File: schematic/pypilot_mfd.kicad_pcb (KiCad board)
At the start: 2 copper layers, 115.8 x 85.9 mm, 94 parts, among them J1 usb, J2 keypad, J3 Conn_01x02, J4 Conn_01x02, J5 jlx256160, J6 usb, Q1 Q_PMOS_GSD, Q2 Q_PMOS_GSD, Q3 Q_PMOS_DSG, Q4 Q_NMOS_GSD, U1 CH340G, U10 24LC512, U11 LMR50410, U12 AP2127K-ADJ, U2 AMS1117-3.3, U3 ESP32-WROOM-32D, U4 SN65220, U5 ADM2587E, U6 LIS2DE12, U7 74AHC04, U8 BUZZER-freetronics_schematic, U9 LIS2DE12, Y1 12mhz

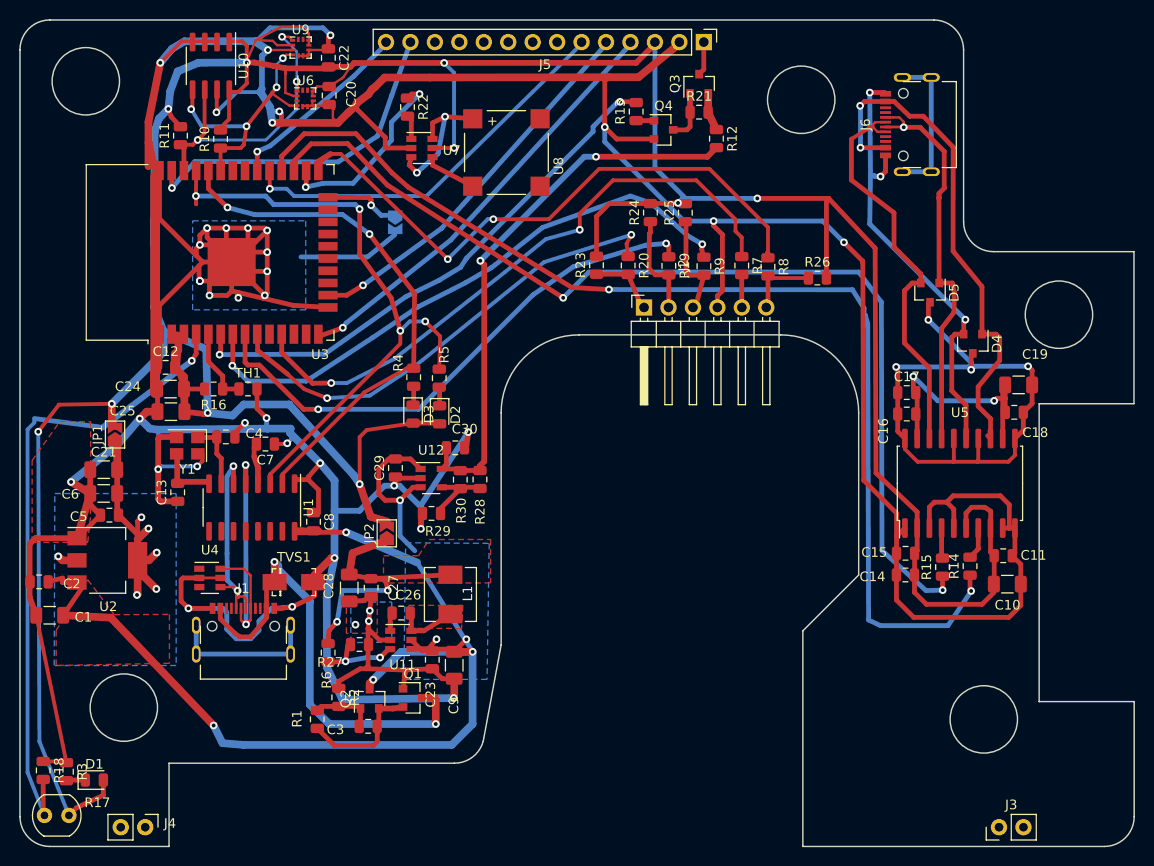
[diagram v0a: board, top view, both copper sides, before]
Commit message: add schematics and models for sensors
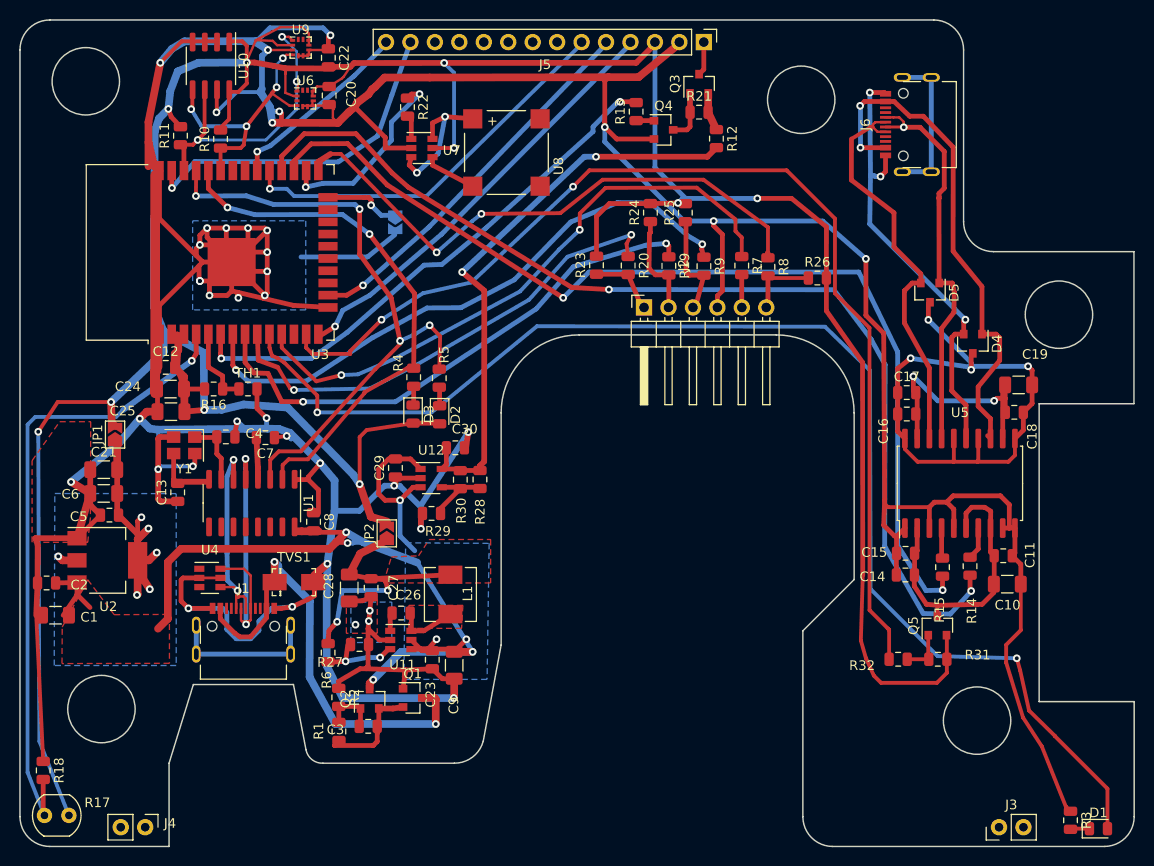
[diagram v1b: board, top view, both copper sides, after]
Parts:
- added Q5: Q_PMOS_DSG, pypilot_footprints:SOT-23_180, F.Cu at (108.1, 77.0)
- added R31: 100k, Resistor_SMD:R_0805_2012Metric, F.Cu at (108.2, 80.5)
- added R32: 10k, Resistor_SMD:R_0805_2012Metric, F.Cu at (104.0, 80.5)
- moved D1 104.4 mm to (124.9, 98.2)
- moved R3 104.4 mm to (122.0, 97.3)
- moved R1 2.58 mm to (46.0, 88.0)
- moved C2 0.78 mm to (15.6, 72.6)
- moved C7 0.67 mm to (38.3, 57.5)
- moved C1 0.60 mm to (16.5, 76.0)
- moved U1 0.46 mm to (36.9, 64.1)
- moved Y1 0.32 mm to (29.9, 58.3)
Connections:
- C10 pad 2: +3V3 -> Net-(C10-Pad2)
- C11 pad 2: +3V3 -> Net-(C10-Pad2)
- C14 pad 2: +3V3 -> Net-(C10-Pad2)
- C15 pad 2: +3V3 -> Net-(C10-Pad2)
- D1 pad 2: +3V3 -> LEDS_VCC
- U3 pad 10: Net-(U3-Pad10) -> LEDS_VCC
- U3 pad 13: Net-(U3-Pad13) -> RS422_PWR
- U5 pad 2: +3V3 -> Net-(C10-Pad2)
- U5 pad 6: +3V3 -> Net-(C10-Pad2)
- U5 pad 8: +3V3 -> Net-(C10-Pad2)
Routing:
- net LEDS_VCC: track 0.00 -> 134.8 mm, vias 0 -> 2
- net RS422_PWR: track 0.00 -> 114.2 mm, vias 0 -> 2
- net Net-(C10-Pad2): track 0.00 -> 30.2 mm
- net +5V: track 134.3 -> 109.4 mm
- net +3V3: track 396.0 -> 374.6 mm
- net TX1: track 116.3 -> 109.2 mm
- net GND: track 660.8 -> 667.8 mm
- net Net-(Q5-Pad1): track 0.00 -> 4.78 mm
- net PWR: track 62.5 -> 60.2 mm
- net Net-(C30-Pad2): track 58.0 -> 59.9 mm
- net Net-(C3-Pad2): track 14.2 -> 12.4 mm
- net RX: track 54.5 -> 55.9 mm
- net PWR_LED: track 64.4 -> 63.0 mm
- net Net-(J1-PadA6): track 29.2 -> 30.5 mm
- net Net-(J1-PadA7): track 21.2 -> 22.4 mm
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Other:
- outline, holes or cut-outs redrawn

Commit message: update enclosures and schematics
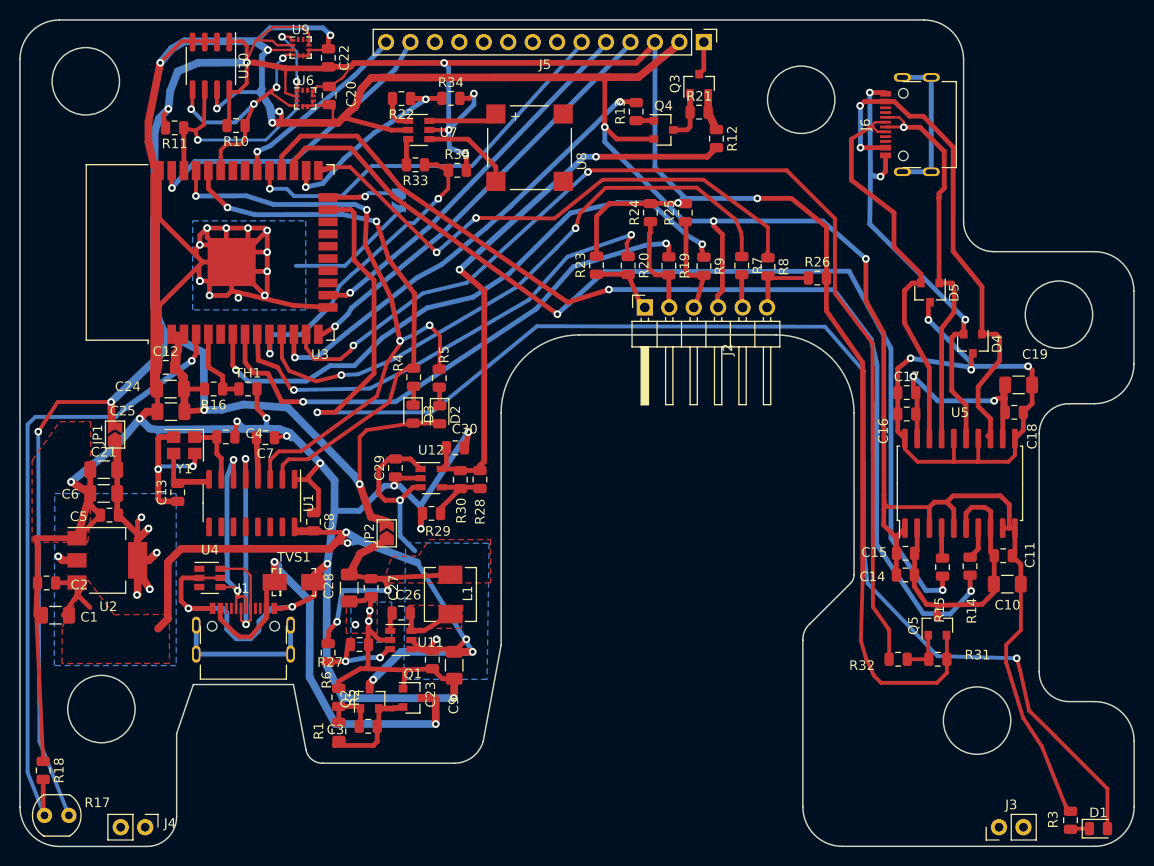
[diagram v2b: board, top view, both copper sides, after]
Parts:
- added R33: 1.2k, Resistor_SMD:R_0805_2012Metric, F.Cu at (53.9, 29.2)
- added R34: 100k, Resistor_SMD:R_0805_2012Metric, F.Cu at (57.6, 22.3)
- added R35: 100k, Resistor_SMD:R_0805_2012Metric, F.Cu at (58.2, 29.8)
- JP3: value Jumper -> Screen Mirrored
- Q3, Q5: value Q_PMOS_DSG -> Q_PMOS_GSD
- U11: footprint Package_TO_SOT_SMD:SOT-23-6 -> pypilot_footprints:SOT-23-6_180
- moved U8 2.45 mm to (65.8, 27.4)
- moved JP3 2.33 mm to (52.2, 32.9)
- moved R10 2.13 mm to (35.3, 25.1), turned to 180 degrees
- moved U7 1.90 mm to (54.2, 25.6)
- moved R22 1.08 mm to (52.5, 22.3), turned to 180 degrees
- moved R11 1.02 mm to (28.9, 25.3), turned to 180 degrees
- moved J2 0.08 mm to (84.1, 44.0), turned to 180 degrees
- turned U11 to 180 degrees
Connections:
- net BUZZER renamed BUZZERA
- U3 pad 10: LEDS_VCC -> BUZZERB
- U3 pad 12: CS_SD -> LEDA
- U3 pad 23: Net-(U3-Pad23) -> LEDS_VCC
- U3 pad 6: LEDA -> Net-(U3-Pad6)
- U7 pad 3: Net-(U7-Pad3) -> Net-(R33-Pad2)
- U7 pad 6: Net-(U7-Pad3) -> Net-(U7-Pad6)
- U8 pad 1: Net-(U7-Pad3) -> Net-(U7-Pad6)
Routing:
- net BUZZERB: track 0.00 -> 33.4 mm, vias 0 -> 2
- net LEDS_VCC: track 134.8 -> 152.1 mm
- net Net-(U7-Pad3): track 14.8 -> 0.00 mm, vias 2 -> 0
- net +3V3: track 374.6 -> 383.8 mm, vias 10 -> 12
- net LEDA: track 56.0 -> 47.8 mm
- net Net-(U7-Pad6): track 0.00 -> 7.20 mm
- net Net-(U7-Pad4): track 5.54 -> 9.60 mm
- net Net-(R33-Pad2): track 0.00 -> 2.74 mm
- net MOSI: track 35.7 -> 33.2 mm
- net BUZZERA: track 20.1 -> 22.3 mm
- net GND: track 667.8 -> 665.8 mm
- net PWR: track 60.2 -> 58.5 mm
- net RX: track 55.9 -> 57.2 mm
- net TX1: track 109.2 -> 110.4 mm
- net SDA: track 28.9 -> 30.0 mm
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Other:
- outline, holes or cut-outs redrawn

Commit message: add foot prints
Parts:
- removed D1: LED3, LED_SMD:LED_0805_2012Metric
- removed JP2: Jumper, Jumper:SolderJumper-2_P1.3mm_Open_TrianglePad1.0x1.5mm
- added C31: 10uF, Capacitor_SMD:C_1206_3216Metric, F.Cu at (51.1, 68.0)
- added Q6: Q_NMOS_GSD, pypilot_footprints:SOT-23_180, F.Cu at (103.5, 85.9)
- added R36: 1.2k, Resistor_SMD:R_0805_2012Metric, F.Cu at (89.6, 73.8)
- added R37: 4.7, Resistor_SMD:R_0805_2012Metric, F.Cu at (99.3, 87.0)
- R3: value 1.5k -> 1.2k
- moved R3 36.0 mm to (95.2, 73.1), turned to 0 degrees
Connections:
- Q5 pad 2: +3V3 -> Net-(Q5-Pad2)
- R14 pad 1: TX1 -> TX2
- R15 pad 1: RX1 -> GND
- R3 pad 1: GND -> Net-(R3-Pad1)
- R3 pad 2: Net-(D1-Pad1) -> Net-(R3-Pad2)
- R31 pad 2: +3V3 -> Net-(Q5-Pad2)
- R32 pad 2: Net-(Q5-Pad1) -> Net-(Q6-Pad1)
- U3 pad 23: LEDS_VCC -> RX1
- U3 pad 24: Net-(JP3-Pad1) -> TX1
- U3 pad 27: RX1 -> RX2
- U3 pad 28: TX1 -> TX2
- U3 pad 6: Net-(U3-Pad6) -> Net-(JP3-Pad1)
- U5 pad 4: Net-(R15-Pad2) -> Net-(R3-Pad2)
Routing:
- net LEDS_VCC: track 152.1 -> 0.00 mm, vias 2 -> 0
- net TX2: track 0.00 -> 110.4 mm, vias 0 -> 2
- net TX1: track 110.4 -> 0.00 mm, vias 2 -> 0
- net GND: track 665.8 -> 640.1 mm
- net +3V3: track 383.8 -> 366.7 mm
- net Net-(C27-Pad2): track 29.4 -> 23.8 mm
- net Net-(Q5-Pad2): track 0.00 -> 2.52 mm
- net Net-(Q5-Pad1): track 4.78 -> 2.53 mm
- net Net-(D1-Pad1): track 1.99 -> 0.00 mm

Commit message: update enclosure
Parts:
- removed JP3: Screen Mirrored, Jumper:SolderJumper-2_P1.3mm_Open_TrianglePad1.0x1.5mm
- added JP2: Jumper, Jumper:SolderJumper-2_P1.3mm_Open_TrianglePad1.0x1.5mm, B.Cu at (47.4, 57.8)
- added R38: 4.7, Resistor_SMD:R_0805_2012Metric, F.Cu at (98.1, 79.8)
- moved R36 23.0 mm to (112.5, 75.7), turned to 180 degrees
- moved R3 13.6 mm to (108.5, 70.5), turned to 90 degrees
- moved R15 8.85 mm to (113.4, 78.5), turned to 180 degrees
- moved R31 2.81 mm to (107.2, 77.9)
- moved Q5 2.58 mm to (106.9, 74.8)
- moved R37 2.40 mm to (101.0, 85.4)
- moved Q6 2.32 mm to (105.2, 84.4)
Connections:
- R3 pad 1: Net-(R3-Pad1) -> Net-(R15-Pad2)
- R36 pad 2: Net-(R3-Pad1) -> Net-(R15-Pad2)
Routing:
- net RX2: track 0.00 -> 115.2 mm, vias 0 -> 2
- net RX1: track 105.8 -> 0.00 mm, vias 2 -> 0
- net +5V: track 109.4 -> 196.4 mm, vias 7 -> 9
- net +3V3: track 366.7 -> 315.0 mm
- net GND: track 640.1 -> 669.8 mm, vias 39 -> 42
- net Net-(C27-Pad2): track 23.8 -> 39.6 mm, vias 2 -> 3
- net Net-(Q5-Pad2): track 2.52 -> 17.8 mm, vias 0 -> 2
- net TX1: track 0.00 -> 7.58 mm, vias 0 -> 1
- net Net-(U3-Pad6): track 7.58 -> 0.00 mm, vias 1 -> 0
- net Net-(Q5-Pad1): track 2.53 -> 9.30 mm
- net Net-(R15-Pad2): track 3.16 -> 8.67 mm
- net TX2: track 110.4 -> 115.5 mm
- net Net-(Q6-Pad1): track 0.00 -> 3.30 mm
- net Net-(C10-Pad2): track 30.2 -> 27.5 mm, vias 0 -> 2
- net Net-(R3-Pad2): track 0.00 -> 2.63 mm
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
